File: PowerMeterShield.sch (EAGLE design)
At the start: 34 parts, among them U1 INA170EA/2K5, U2 THS4521, U3 INA138, U4 ADUM1250ARZ, U5 MCP3426A0-E/SN, U6 ISL21080

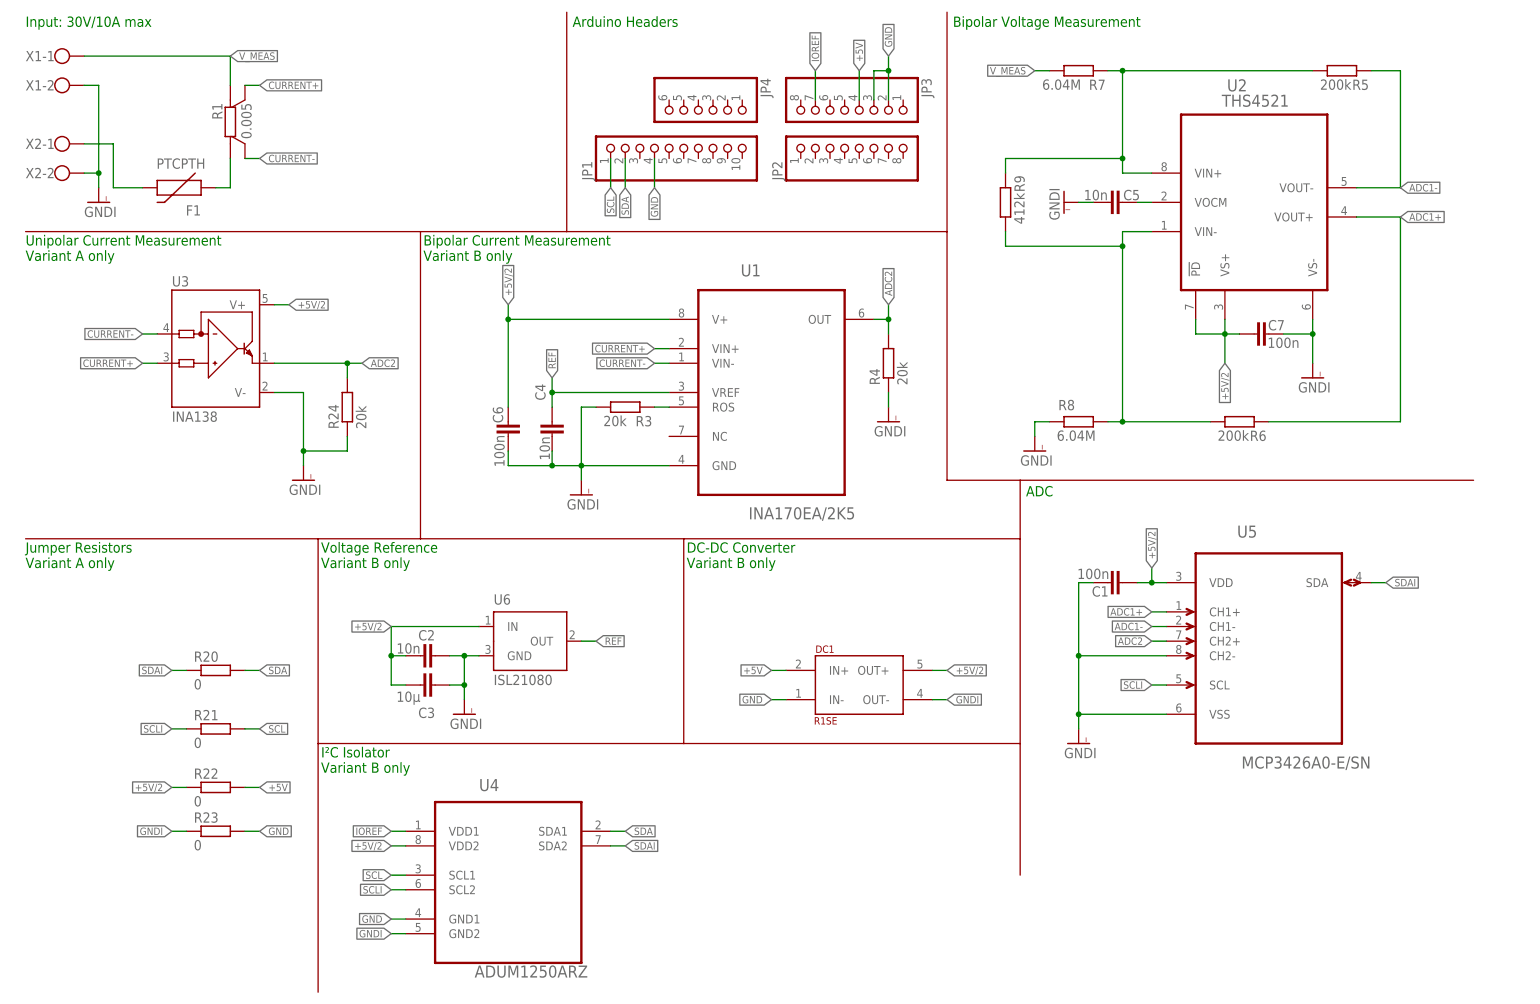
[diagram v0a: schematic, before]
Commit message: Added prices + order codes
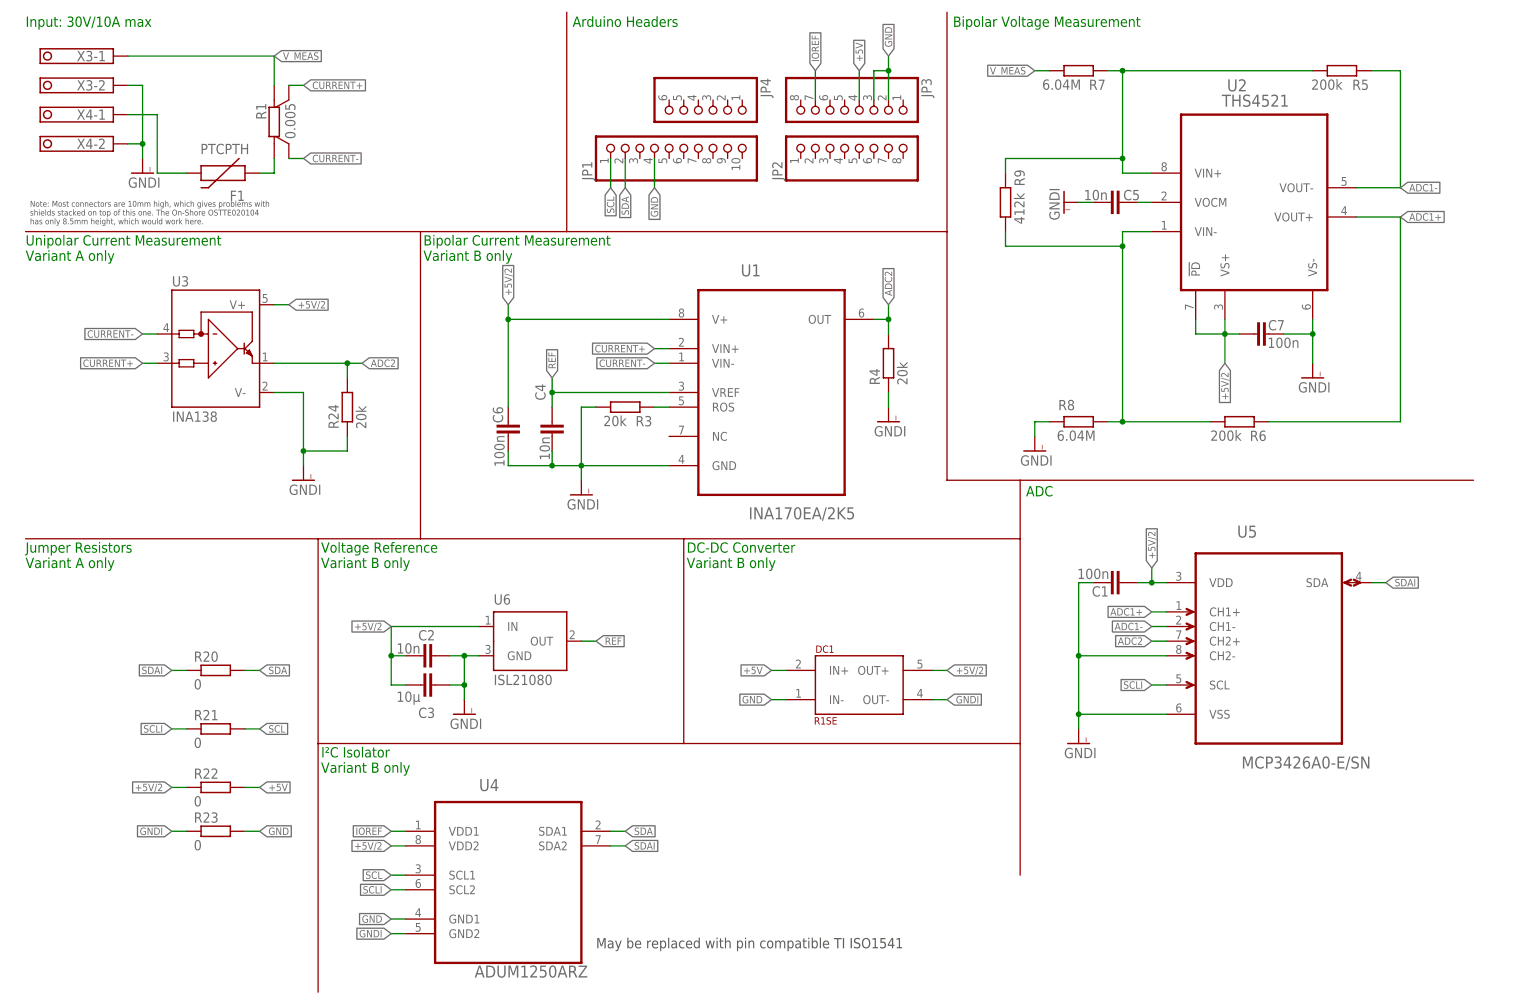
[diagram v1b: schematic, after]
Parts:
- removed X1, X2: (no value), con-wago-500:W237-102
- added X3, X4: 1751248, con-phoenix-350:1751248
- DC1: OC_DIGIKEY (none) -> 945-1659-1-ND; PRICE_10 (none) -> 3.08; PRICE_100 (none) -> 2.82
- F1: PRICE_100 (none) -> 0.53
- R1: PRICE_10 0.844 -> 0.90; PRICE_100 (none) -> 0.78
- R20: OC_DIGIKEY (none) -> 1276-5994-1-ND; PRICE_10 (none) -> 0.08; PRICE_100 (none) -> 0.034
- R21, R22: OC_DIGIKEY (none) -> 1276-5994-1-ND; PRICE_10 (none) -> 0.082; PRICE_100 (none) -> 0.034
- R23: OC_DIGIKEY (none) -> 1276-5994-1-ND; PRICE_10 (none) -> 0.082; PRICE_100 (none) -> 0.032
- R24, R3, R4: OC_FARNELL (none) -> 2129219; PRICE_5000 (none) -> 0.001
- R5, R6: OC_FARNELL (none) -> 2129299; PRICE_5000 (none) -> 0.001
- R7: OC_DIGIKEY (none) -> 311-6.04MCRCT-ND; PRICE_10 (none) -> 0.013; PRICE_100 (none) -> 0.008
- R8: OC_DIGIKEY (none) -> 311-6.04MCRCT-ND; PRICE_10 (none) -> 0.013; PRICE_100 (none) -> 0.0083
- R9: OC_DIGIKEY (none) -> 311-412KCRCT-ND; PRICE_10 (none) -> 0.015; PRICE_100 (none) -> 0.0071
- U1: OC_DIGIKEY (none) -> INA170EA/2K5CT-ND; OC_FARNELL (none) -> 1234851; PRICE_10 (none) -> 1.85; PRICE_100 (none) -> 0.92; REMARK (none) -> USE DIGIKEY FOR 100
- U2: OC_DIGIKEY (none) -> 296-35973-1-ND; OC_FARNELL (none) -> 1755708; PRICE_10 (none) -> 1.81; PRICE_100 (none) -> 1.17; REMARK (none) -> USE DIGIKEY FOR 100
- U3: OC_DIGIKEY (none) -> 296-17936-1-ND; PRICE_10 (none) -> 1.15; PRICE_100 (none) -> 0.63; REMARK (none) -> USE DIGIKEY FOR 100
- U4: OC_DIGIKEY (none) -> 296-34872-1-ND; PRICE_10 (none) -> 3.33; PRICE_100 (none) -> 1.74
- U5: OC_DIGIKEY (none) -> MCP3426A0-E/SN-ND; PRICE_100 (none) -> 1.58
- U6: OC_DIGIKEY (none) -> ISL21080DIH310Z-TKCT-ND; PRICE_10 (none) -> 1.35; PRICE_100 (none) -> 0.81
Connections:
- net GNDI: now also X3-2.K, X4-2.K; no longer X1-2.KL, X2-2.KL
- net VIN_MEAS: now also X4-1.K; no longer X2-1.KL
- net V_MEAS: now also X3-1.K; no longer X1-1.KL
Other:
- note added: "May be replaced with pin compatible TI ISO1541"
- note added: "Note: Most connectors are 10mm high, which gives problems with shields stacked on top of this one. The On-Shore OSTTE020104 has only 8.5mm height, which would work here."
- moved on the sheet: F1, R1

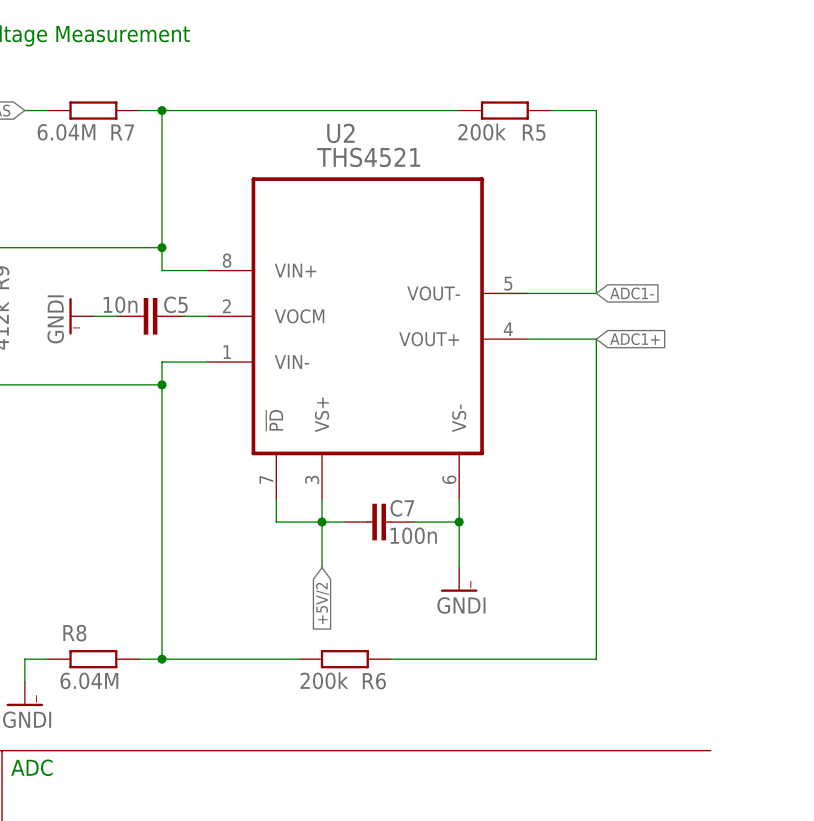
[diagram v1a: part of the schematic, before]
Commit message: Added experimental serial line resistors and capacitors
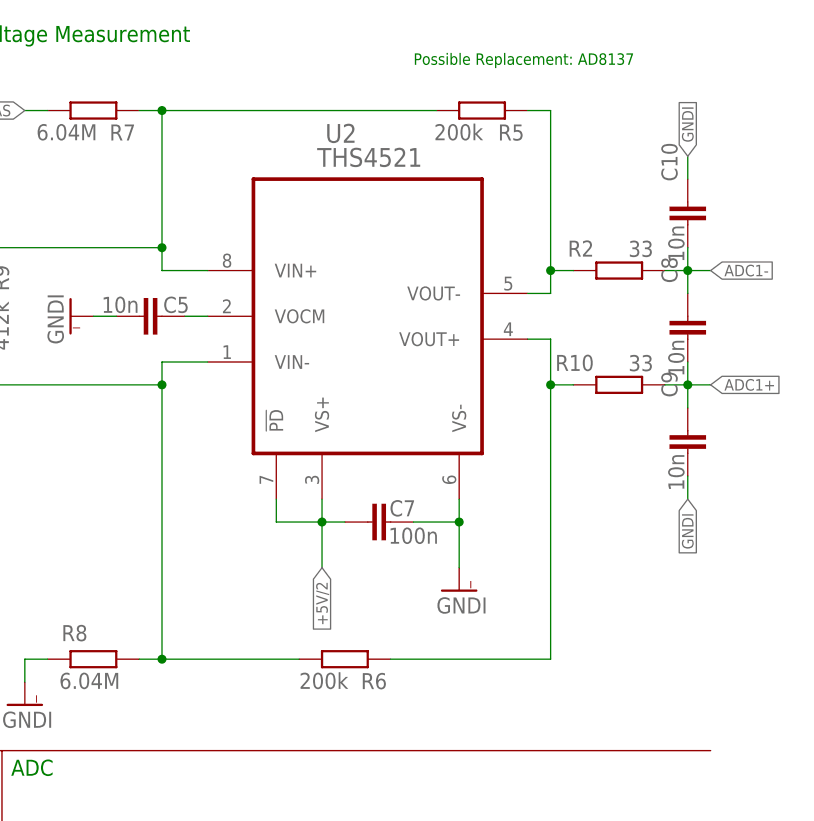
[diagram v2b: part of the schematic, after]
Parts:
- added C10, C8, C9: 10n, rcl:C-EUC0805
- added R10, R2: 33, rcl:R-EU_R0805
- R20: OC_TME (none) -> SMD2010-0R
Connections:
- new net ADC1+_OLD: R10.2, R6.2, U2.VOUT+
- new net ADC1-_OLD: R2.2, R5.2, U2.VOUT-
- net ADC1+: now also C8.1, C9.2, R10.1; no longer R6.2, U2.VOUT+
- net ADC1-: now also C10.1, C8.2, R2.1; no longer R5.2, U2.VOUT-
- net GNDI: now also C10.2, C9.1
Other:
- note added: "Possible Replacement: AD8137"
- moved on the sheet: R5
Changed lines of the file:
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@@
 <part name="R20" library="rcl" deviceset="R-EU_" device="R2010" value="0">
 <attribute name="OC_DIGIKEY" value="1276-5994-1-ND"/>
+<attribute name="OC_TME" value="SMD2010-0R"/>
 <attribute name="PRICE_10" value="0.08"/>
 <attribute name="PRICE_100" value="0.034"/>
@@
 <attribute name="PRICE_10" value="0.27"/>
 <attribute name="PRICE_100" value="0.19"/>
+</part>
+<part name="C8" library="rcl" deviceset="C-EU" device="C0805" value="10n">
+<attribute name="OC_FARNELL" value="2310707"/>
+<attribute name="PRICE_100" value="0.005"/>
+</part>
+<part name="R2" library="rcl" deviceset="R-EU_" device="R0805" value="33">
+<attribute name="OC_DIGIKEY" value="311-412KCRCT-ND"/>
+<attribute name="PRICE_10" value="0.015"/>
+<attribute name="PRICE_100" value="0.0071"/>
+</part>
+<part name="R10" library="rcl" deviceset="R-EU_" device="R0805" value="33">
+<attribute name="OC_DIGIKEY" value="311-412KCRCT-ND"/>
+<attribute name="PRICE_10" value="0.015"/>
+<attribute name="PRICE_100" value="0.0071"/>
+</part>
+<part name="C9" library="rcl" deviceset="C-EU" device="C0805" value="10n">
+<attribute name="OC_FARNELL" value="2310707"/>
+<attribute name="PRICE_100" value="0.005"/>
+</part>
+<part name="C10" library="rcl" deviceset="C-EU" device="C0805" value="10n">
+<attribute name="OC_FARNELL" value="2310707"/>
+<attribute name="PRICE_100" value="0.005"/>
 </part>
 </parts>
@@
 has only 8.5mm height, which would work here.</text>
 <text x="104.14" y="12.7" size="1.778" layer="97">May be replaced with pin compatible TI ISO1541</text>
+<text x="223.52" y="170.18" size="1.27" layer="91">Possible Replacement: AD8137</text>
 </plain>
 <instances>
@@
 <attribute name="OC_DIGIKEY" x="187.96" y="104.14" size="1.778" layer="96" display="off"/>
 </instance>
-<instance part="R5" gate="G$1" x="233.68" y="165.1" smashed="yes">
-<attribute name="NAME" x="235.458" y="161.7726" size="1.778" layer="95"/>
-<attribute name="VALUE" x="228.346" y="161.798" size="1.778" layer="96"/>
-<attribute name="PRICE_5000" x="233.68" y="165.1" size="1.778" layer="96" display="off"/>
-<attribute name="OC_FARNELL" x="233.68" y="165.1" size="1.778" layer="96" display="off"/>
+<instance part="R5" gate="G$1" x="231.14" y="165.1" smashed="yes">
+<attribute name="NAME" x="232.918" y="161.7726" size="1.778" layer="95"/>
+<attribute name="VALUE" x="225.806" y="161.798" size="1.778" layer="96"/>
+<attribute name="PRICE_5000" x="231.14" y="165.1" size="1.778" layer="96" display="off"/>
+<attribute name="OC_FARNELL" x="231.14" y="165.1" size="1.778" layer="96" display="off"/>
 </instance>
 <instance part="R6" gate="G$1" x="215.9" y="104.14" smashed="yes">
@@
 <attribute name="PRICE_10" x="38.1" y="60.96" size="1.778" layer="96" display="off"/>
 <attribute name="OC_DIGIKEY" x="38.1" y="60.96" size="1.778" layer="96" display="off"/>
+<attribute name="OC_TME" x="38.1" y="60.96" size="1.778" layer="96" display="off"/>
 </instance>
 <instance part="R21" gate="G$1" x="38.1" y="50.8">
@@
 <instance part="X4" gate="-2" x="20.32" y="152.4" smashed="yes" rot="R180">
 <attribute name="NAME" x="19.05" y="153.289" size="1.778" layer="95" font="vector" rot="R180"/>
+</instance>
+<instance part="C8" gate="G$1" x="254" y="139.7" smashed="yes" rot="R180">
+<attribute name="NAME" x="251.079" y="148.844" size="1.778" layer="95" rot="R270"/>
+<attribute name="VALUE" x="251.841" y="139.7" size="1.778" layer="96" rot="R270"/>
+<attribute name="PRICE_100" x="254" y="139.7" size="1.27" layer="96" rot="R180" display="off"/>
+<attribute name="OC_FARNELL" x="254" y="139.7" size="1.27" layer="96" rot="R180" display="off"/>
+</instance>
+<instance part="R2" gate="G$1" x="246.38" y="147.32" smashed="yes" rot="R180">
+<attribute name="NAME" x="243.586" y="150.6474" size="1.778" layer="95" rot="R180"/>
+<attribute name="VALUE" x="250.19" y="150.622" size="1.778" layer="96" rot="R180"/>
+<attribute name="PRICE_100" x="246.38" y="147.32" size="1.778" layer="96" rot="R180" display="off"/>
+<attribute name="PRICE_10" x="246.38" y="147.32" size="1.778" layer="96" rot="R180" display="off"/>
+<attribute name="OC_DIGIKEY" x="246.38" y="147.32" size="1.778" layer="96" rot="R180" display="off"/>
+</instance>
+<instance part="R10" gate="G$1" x="246.38" y="134.62" smashed="yes" rot="R180">
+<attribute name="NAME" x="243.586" y="137.9474" size="1.778" layer="95" rot="R180"/>
+<attribute name="VALUE" x="250.19" y="137.922" size="1.778" layer="96" rot="R180"/>
+<attribute name="PRICE_100" x="246.38" y="134.62" size="1.778" layer="96" rot="R180" display="off"/>
+<attribute name="PRICE_10" x="246.38" y="134.62" size="1.778" layer="96" rot="R180" display="off"/>
+<attribute name="OC_DIGIKEY" x="246.38" y="134.62" size="1.778" layer="96" rot="R180" display="off"/>
+</instance>
+<instance part="C9" gate="G$1" x="254" y="127" smashed="yes" rot="R180">
+<attribute name="NAME" x="251.079" y="136.144" size="1.778" layer="95" rot="R270"/>
+<attribute name="VALUE" x="251.841" y="127" size="1.778" layer="96" rot="R270"/>
+<attribute name="PRICE_100" x="254" y="127" size="1.27" layer="96" rot="R180" display="off"/>
+<attribute name="OC_FARNELL" x="254" y="127" size="1.27" layer="96" rot="R180" display="off"/>
+</instance>
+<instance part="C10" gate="G$1" x="254" y="152.4" smashed="yes" rot="R180">
+<attribute name="NAME" x="251.079" y="161.544" size="1.778" layer="95" rot="R270"/>
+<attribute name="VALUE" x="251.841" y="152.4" size="1.778" layer="96" rot="R270"/>
+<attribute name="PRICE_100" x="254" y="152.4" size="1.27" layer="96" rot="R180" display="off"/>
+<attribute name="OC_FARNELL" x="254" y="152.4" size="1.27" layer="96" rot="R180" display="off"/>
 </instance>
 </instances>
@@
 <label x="30.48" y="33.02" size="1.27" layer="95" rot="R180" xref="yes"/>
 </segment>
+<segment>
+<pinref part="C10" gate="G$1" pin="2"/>
+<wire x1="254" y1="157.48" x2="254" y2="160.02" width="0.1524" layer="91"/>
+<label x="254" y="160.02" size="1.27" layer="95" rot="R90" xref="yes"/>
+</segment>
+<segment>
+<pinref part="C9" gate="G$1" pin="1"/>
+<wire x1="254" y1="124.46" x2="254" y2="121.92" width="0.1524" layer="91"/>
+<label x="254" y="121.92" size="1.27" layer="95" rot="R270" xref="yes"/>
+</segment>
 </net>
 <net name="+5V/2" class="0">
@@
 </segment>
 <segment>
-<pinref part="R6" gate="G$1" pin="2"/>
-<wire x1="220.98" y1="104.14" x2="243.84" y2="104.14" width="0.1524" layer="91"/>
-<wire x1="243.84" y1="104.14" x2="243.84" y2="139.7" width="0.1524" layer="91"/>
-<pinref part="U2" gate="A" pin="VOUT+"/>
-<wire x1="243.84" y1="139.7" x2="236.22" y2="139.7" width="0.1524" layer="91"/>
-<label x="243.84" y="139.7" size="1.27" layer="95" xref="yes"/>
+<pinref part="C8" gate="G$1" pin="1"/>
+<wire x1="254" y1="137.16" x2="254" y2="134.62" width="0.1524" layer="91"/>
+<pinref part="R10" gate="G$1" pin="1"/>
+<wire x1="254" y1="134.62" x2="251.46" y2="134.62" width="0.1524" layer="91"/>
+<wire x1="254" y1="134.62" x2="256.54" y2="134.62" width="0.1524" layer="91"/>
+<junction x="254" y="134.62"/>
+<label x="256.54" y="134.62" size="1.27" layer="95" xref="yes"/>
+<pinref part="C9" gate="G$1" pin="2"/>
+<wire x1="254" y1="134.62" x2="254" y2="132.08" width="0.1524" layer="91"/>
 </segment>
 </net>
@@
 </segment>
 <segment>
-<pinref part="U2" gate="A" pin="VOUT-"/>
-<wire x1="236.22" y1="144.78" x2="243.84" y2="144.78" width="0.1524" layer="91"/>
-<wire x1="243.84" y1="144.78" x2="243.84" y2="165.1" width="0.1524" layer="91"/>
-<pinref part="R5" gate="G$1" pin="2"/>
-<wire x1="243.84" y1="165.1" x2="238.76" y2="165.1" width="0.1524" layer="91"/>
-<label x="243.84" y="144.78" size="1.27" layer="95" xref="yes"/>
+<pinref part="R2" gate="G$1" pin="1"/>
+<pinref part="C8" gate="G$1" pin="2"/>
+<wire x1="251.46" y1="147.32" x2="254" y2="147.32" width="0.1524" layer="91"/>
+<wire x1="254" y1="147.32" x2="254" y2="144.78" width="0.1524" layer="91"/>
+<wire x1="254" y1="147.32" x2="256.54" y2="147.32" width="0.1524" layer="91"/>
+<junction x="254" y="147.32"/>
+<label x="256.54" y="147.32" size="1.27" layer="95" xref="yes"/>
+<pinref part="C10" gate="G$1" pin="1"/>
+<wire x1="254" y1="147.32" x2="254" y2="149.86" width="0.1524" layer="91"/>
 </segment>
 </net>
@@
 <pinref part="R5" gate="G$1" pin="1"/>
 <wire x1="195.58" y1="149.86" x2="195.58" y2="165.1" width="0.1524" layer="91"/>
-<wire x1="195.58" y1="165.1" x2="228.6" y2="165.1" width="0.1524" layer="91"/>
+<wire x1="195.58" y1="165.1" x2="226.06" y2="165.1" width="0.1524" layer="91"/>
 <pinref part="R9" gate="G$1" pin="2"/>
 <wire x1="175.26" y1="147.32" x2="175.26" y2="149.86" width="0.1524" layer="91"/>
@@
 </segment>
 </net>
+<net name="ADC1+_OLD" class="0">
+<segment>
+<pinref part="R6" gate="G$1" pin="2"/>
+<wire x1="220.98" y1="104.14" x2="238.76" y2="104.14" width="0.1524" layer="91"/>
+<wire x1="238.76" y1="104.14" x2="238.76" y2="134.62" width="0.1524" layer="91"/>
+<pinref part="U2" gate="A" pin="VOUT+"/>
+<wire x1="238.76" y1="134.62" x2="238.76" y2="139.7" width="0.1524" layer="91"/>
+<wire x1="238.76" y1="139.7" x2="236.22" y2="139.7" width="0.1524" layer="91"/>
+<pinref part="R10" gate="G$1" pin="2"/>
+<wire x1="241.3" y1="134.62" x2="238.76" y2="134.62" width="0.1524" layer="91"/>
+<junction x="238.76" y="134.62"/>
+</segment>
+</net>
+<net name="ADC1-_OLD" class="0">
+<segment>
+<pinref part="U2" gate="A" pin="VOUT-"/>
+<wire x1="236.22" y1="144.78" x2="238.76" y2="144.78" width="0.1524" layer="91"/>
+<wire x1="238.76" y1="144.78" x2="238.76" y2="147.32" width="0.1524" layer="91"/>
+<pinref part="R5" gate="G$1" pin="2"/>
+<wire x1="238.76" y1="147.32" x2="238.76" y2="165.1" width="0.1524" layer="91"/>
+<wire x1="238.76" y1="165.1" x2="236.22" y2="165.1" width="0.1524" layer="91"/>
+<pinref part="R2" gate="G$1" pin="2"/>
+<wire x1="241.3" y1="147.32" x2="238.76" y2="147.32" width="0.1524" layer="91"/>
+<junction x="238.76" y="147.32"/>
+</segment>
+</net>
